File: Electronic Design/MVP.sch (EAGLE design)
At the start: 38 parts, among them IC1 ACS711KLCTR-12AB-T, IC3 ATMEGA328-PU, Q2 16MHz, Q3 IRF9540, Q4 IRF9540

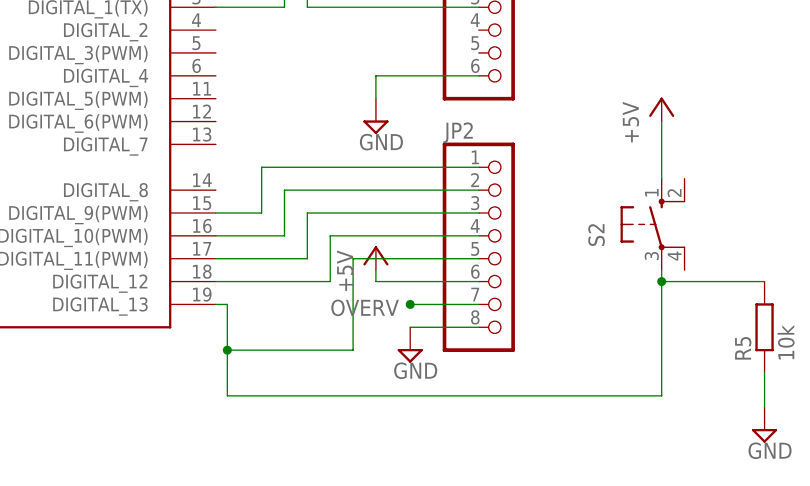
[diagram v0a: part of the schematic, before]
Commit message: Changed position of 5V and overvoltage on JP2
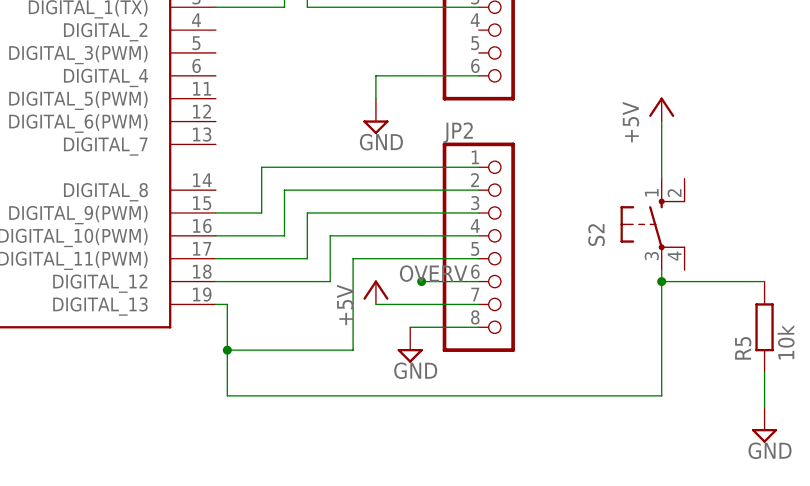
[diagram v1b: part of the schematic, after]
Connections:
- net +5V: now also JP2.7; no longer JP2.6
- net OVERV: now also JP2.6; no longer JP2.7
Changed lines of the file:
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@@
 <?xml version="1.0" encoding="utf-8"?>
 <!DOCTYPE eagle SYSTEM "eagle.dtd">
-<eagle version="7.6.0">
+<eagle version="7.5.0">
 <drawing>
 <settings>
@@
 <instance part="R5" gate="G$1" x="48.26" y="-10.16" rot="R90"/>
 <instance part="SUPPLY3" gate="GND" x="48.26" y="-21.59"/>
-<instance part="+5V3" gate="1" x="5.08" y="-1.27"/>
+<instance part="+5V3" gate="1" x="5.08" y="-5.08"/>
 <instance part="POT1" gate="G$1" x="-40.64" y="71.12" smashed="yes" rot="MR180">
 <attribute name="NAME" x="-39.37" y="65.151" size="1.778" layer="95" rot="MR180"/>
@@
 <segment>
 <pinref part="+5V3" gate="1" pin="+5V"/>
-<wire x1="5.08" y1="-3.81" x2="5.08" y2="-5.08" width="0.1524" layer="91"/>
-<pinref part="JP2" gate="A" pin="6"/>
-<wire x1="5.08" y1="-5.08" x2="16.51" y2="-5.08" width="0.1524" layer="91"/>
+<pinref part="JP2" gate="A" pin="7"/>
+<wire x1="5.08" y1="-7.62" x2="16.51" y2="-7.62" width="0.1524" layer="91"/>
 </segment>
 </net>
@@
 </segment>
 <segment>
-<pinref part="JP2" gate="A" pin="7"/>
-<wire x1="16.51" y1="-7.62" x2="8.89" y2="-7.62" width="0.1524" layer="91"/>
-<junction x="8.89" y="-7.62"/>
-<label x="0" y="-8.89" size="1.778" layer="95"/>
-</segment>
-</net>
+<pinref part="JP2" gate="A" pin="6"/>
+<wire x1="16.51" y1="-5.08" x2="10.16" y2="-5.08" width="0.1524" layer="91"/>
+<junction x="10.16" y="-5.08"/>
+<label x="7.62" y="-5.08" size="1.778" layer="95"/>
+</segment>
+</net>

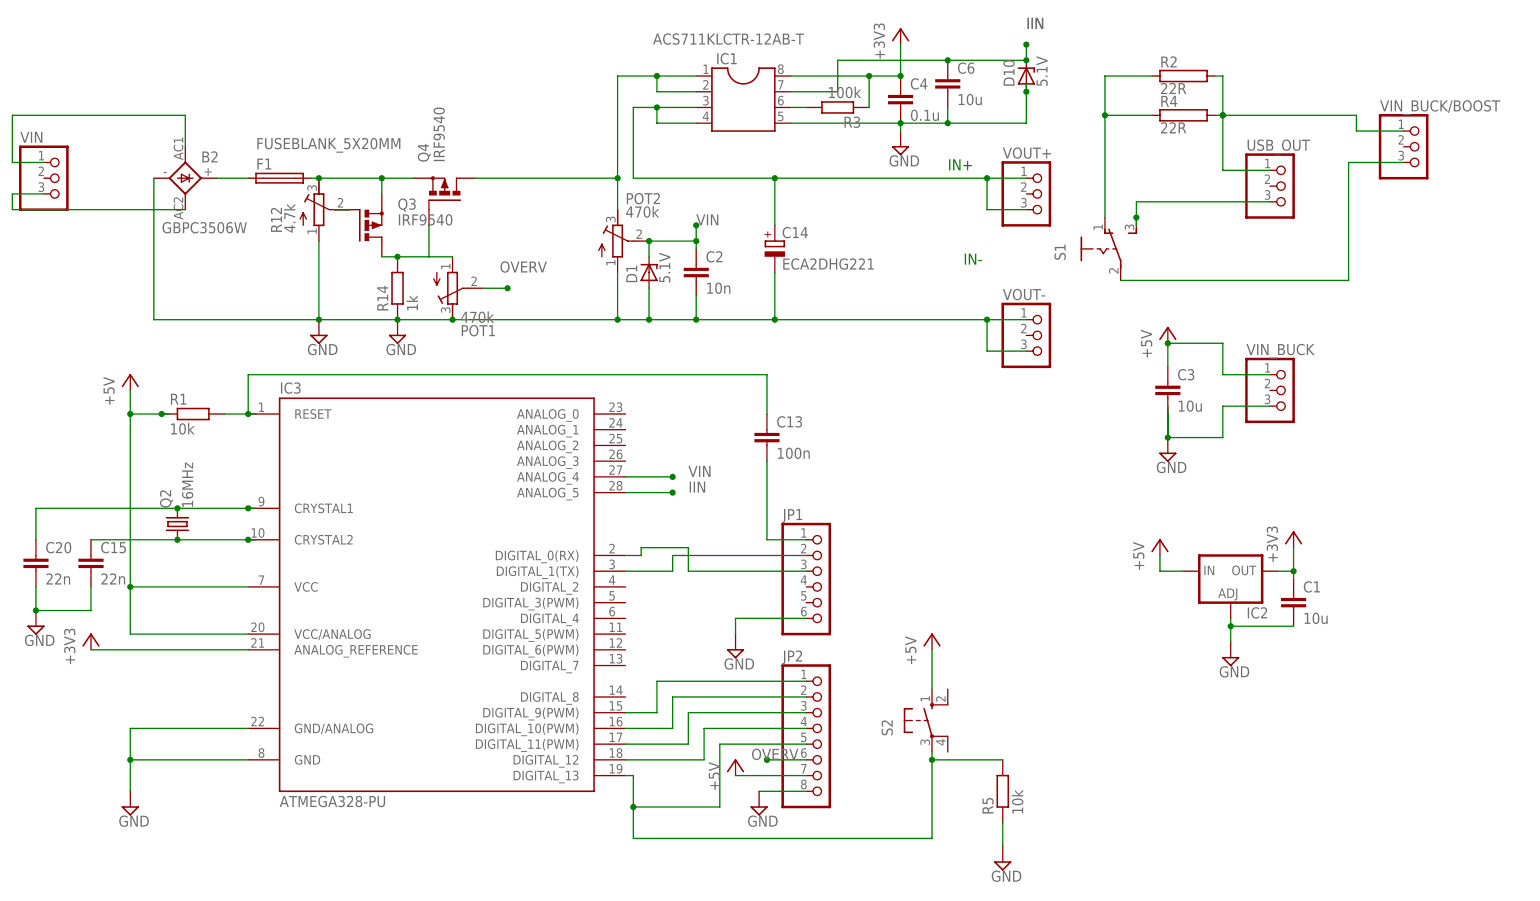
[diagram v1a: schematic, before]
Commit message: Updated circuit to reflect change from ACS711 to ACS712
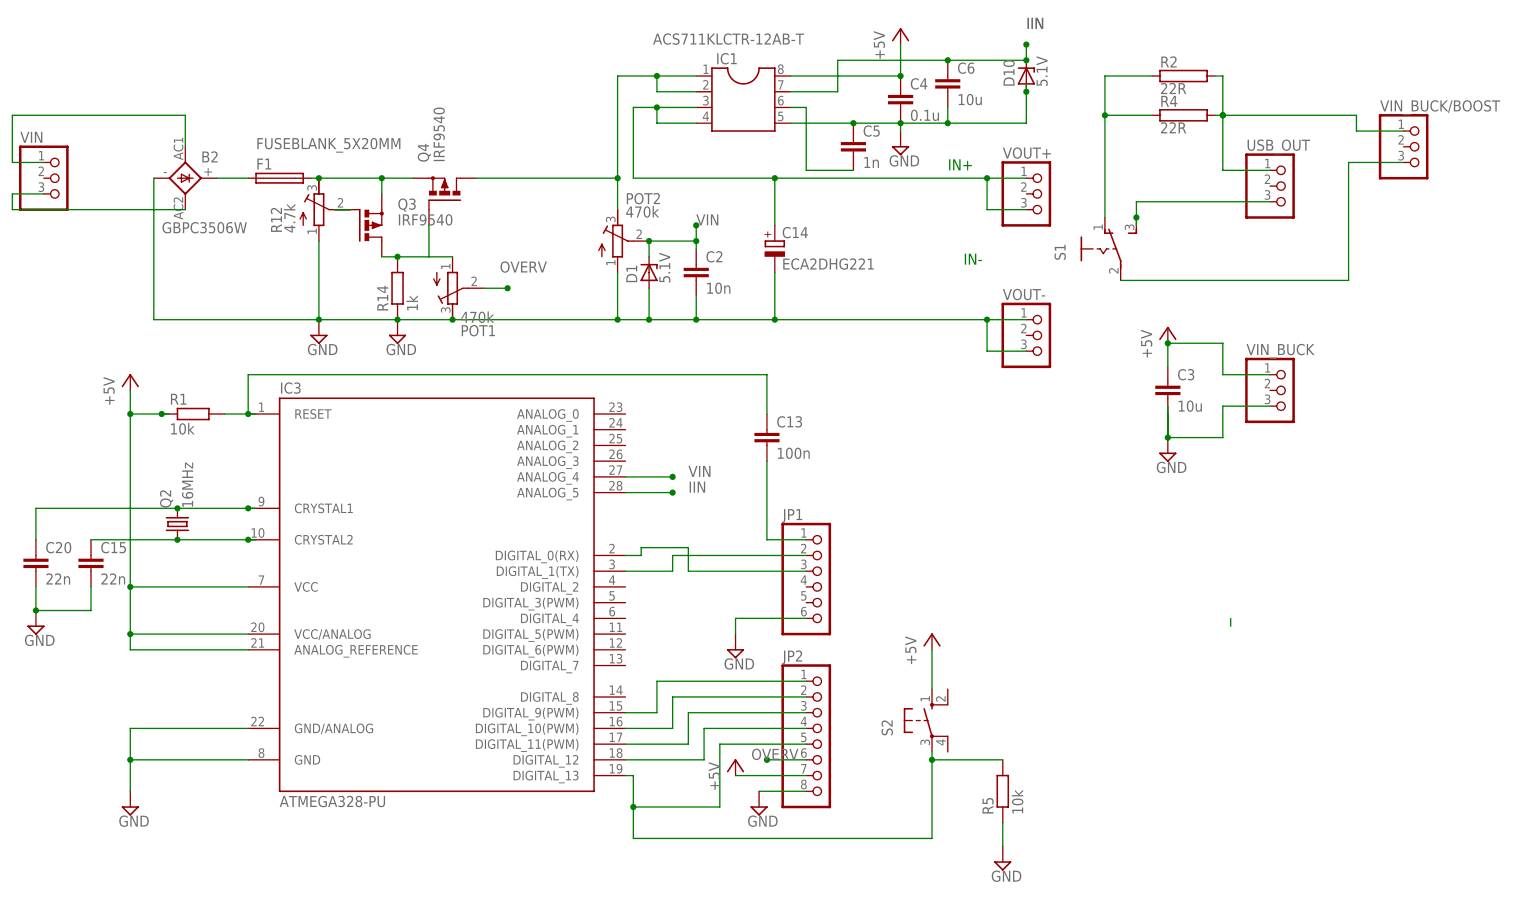
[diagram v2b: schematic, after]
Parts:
- removed C1: 10u, resistor:C-EUC1210
- removed IC2: (no value), v-reg:LM138-TS
- removed R3: 100k, resistor:R-EU_R1210
- added C5: 1n, resistor:C-EUC1210
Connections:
- removed net +3V3: C1.1, C4.1, IC1.8, IC2.OUT, IC3.ANALOG_REFERENCE, R3.1
- net +5V: now also C4.1, IC1.8, IC3.ANALOG_REFERENCE; no longer IC2.IN
- net GND: now also C5.1; no longer C1.2, IC2.ADJ
- net N$2: now also C5.2; no longer R3.2
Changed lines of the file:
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@@
 <part name="C4" library="resistor" deviceset="C-EU" device="C1210" value="0.1u"/>
 <part name="SUPPLY1" library="supply2" deviceset="GND" device=""/>
-<part name="R3" library="resistor" deviceset="R-EU_" device="R1210" value="100k"/>
 <part name="POT2" library="resistor" deviceset="R-TRIMM" device="4G/J" value="470k"/>
 <part name="D10" library="diode" deviceset="ZPD" device="" value="5.1V"/>
@@
 <part name="SUPPLY2" library="supply2" deviceset="GND" device=""/>
 <part name="+3V2" library="supply1" deviceset="+5V" device=""/>
-<part name="IC2" library="v-reg" deviceset="LM138-TS" device=""/>
-<part name="SUPPLY5" library="supply2" deviceset="GND" device=""/>
 <part name="+3V3" library="supply1" deviceset="+5V" device=""/>
-<part name="+3V4" library="supply1" deviceset="+3V3" device=""/>
-<part name="C1" library="resistor" deviceset="C-EU" device="C1210" value="10u"/>
-<part name="+3V1" library="supply1" deviceset="+3V3" device=""/>
-<part name="+3V5" library="supply1" deviceset="+3V3" device=""/>
 <part name="JP1" library="pinhead" deviceset="PINHD-1X6" device=""/>
 <part name="SUPPLY6" library="supply2" deviceset="GND" device=""/>
@@
 <part name="D1" library="diode" deviceset="ZPD" device="" value="5.1V"/>
 <part name="C6" library="resistor" deviceset="C-EU" device="C1210" value="10u"/>
+<part name="C5" library="resistor" deviceset="C-EU" device="C1210" value="1n"/>
 </parts>
 <sheets>
@@
 <instance part="C4" gate="G$1" x="31.75" y="102.87"/>
 <instance part="SUPPLY1" gate="GND" x="31.75" y="93.98"/>
-<instance part="R3" gate="G$1" x="21.59" y="100.33" rot="R180"/>
 <instance part="POT2" gate="G$1" x="-13.97" y="78.74" smashed="yes">
 <attribute name="NAME" x="-12.7" y="84.709" size="1.778" layer="95"/>
@@
 <instance part="SUPPLY2" gate="GND" x="74.93" y="44.45"/>
 <instance part="+3V2" gate="1" x="74.93" y="64.77"/>
-<instance part="IC2" gate="G$1" x="85.09" y="25.4"/>
-<instance part="SUPPLY5" gate="GND" x="85.09" y="11.43"/>
-<instance part="+3V3" gate="1" x="73.66" y="30.48"/>
-<instance part="+3V4" gate="G$1" x="95.25" y="31.75"/>
-<instance part="C1" gate="G$1" x="95.25" y="21.59"/>
-<instance part="+3V1" gate="G$1" x="31.75" y="113.03"/>
-<instance part="+3V5" gate="G$1" x="-99.06" y="15.24"/>
+<instance part="+3V3" gate="1" x="31.75" y="113.03"/>
 <instance part="JP1" gate="A" x="19.05" y="22.86"/>
 <instance part="SUPPLY6" gate="GND" x="5.08" y="12.7"/>
@@
 <instance part="D1" gate="G$1" x="-8.89" y="73.66" rot="R90"/>
 <instance part="C6" gate="G$1" x="39.37" y="105.41"/>
+<instance part="C5" gate="G$1" x="24.13" y="95.25"/>
 </instances>
 <busses>
@@
 <junction x="39.37" y="97.79"/>
 <pinref part="IC1" gate="G$1" pin="5"/>
-<wire x1="13.97" y1="97.79" x2="31.75" y2="97.79" width="0.1524" layer="91"/>
+<wire x1="13.97" y1="97.79" x2="24.13" y2="97.79" width="0.1524" layer="91"/>
+<wire x1="24.13" y1="97.79" x2="31.75" y2="97.79" width="0.1524" layer="91"/>
 <wire x1="31.75" y1="97.79" x2="31.75" y2="96.52" width="0.1524" layer="91"/>
 <pinref part="C6" gate="G$1" pin="2"/>
+<pinref part="C5" gate="G$1" pin="1"/>
+<junction x="24.13" y="97.79"/>
 </segment>
 <segment>
@@
 <pinref part="VIN_BUCK" gate="A" pin="3"/>
 <wire x1="83.82" y1="52.07" x2="91.44" y2="52.07" width="0.1524" layer="91"/>
-</segment>
-<segment>
-<pinref part="IC2" gate="G$1" pin="ADJ"/>
-<wire x1="85.09" y1="17.78" x2="85.09" y2="16.51" width="0.1524" layer="91"/>
-<pinref part="C1" gate="G$1" pin="2"/>
-<wire x1="85.09" y1="16.51" x2="85.09" y2="13.97" width="0.1524" layer="91"/>
-<wire x1="95.25" y1="16.51" x2="85.09" y2="16.51" width="0.1524" layer="91"/>
-<junction x="85.09" y="16.51"/>
-<pinref part="SUPPLY5" gate="GND" pin="GND"/>
 </segment>
 <segment>
@@
 <junction x="-87.63" y="50.8"/>
 <junction x="-92.71" y="50.8"/>
+<pinref part="IC3" gate="1" pin="ANALOG_REFERENCE"/>
+<wire x1="-73.66" y1="12.7" x2="-92.71" y2="12.7" width="0.1524" layer="91"/>
+<wire x1="-92.71" y1="12.7" x2="-92.71" y2="15.24" width="0.1524" layer="91"/>
+<junction x="-92.71" y="15.24"/>
 </segment>
 <segment>
@@
 </segment>
 <segment>
-<pinref part="IC2" gate="G$1" pin="IN"/>
-<pinref part="+3V3" gate="1" pin="+5V"/>
-<wire x1="77.47" y1="25.4" x2="73.66" y2="25.4" width="0.1524" layer="91"/>
-<wire x1="73.66" y1="25.4" x2="73.66" y2="27.94" width="0.1524" layer="91"/>
-</segment>
-<segment>
 <pinref part="S2" gate="1" pin="S"/>
 <pinref part="+5V2" gate="1" pin="+5V"/>
@@
 <wire x1="5.08" y1="-7.62" x2="16.51" y2="-7.62" width="0.1524" layer="91"/>
 </segment>
+<segment>
+<pinref part="C4" gate="G$1" pin="1"/>
+<wire x1="31.75" y1="105.41" x2="31.75" y2="110.49" width="0.1524" layer="91"/>
+<junction x="31.75" y="105.41"/>
+<pinref part="IC1" gate="G$1" pin="8"/>
+<wire x1="13.97" y1="105.41" x2="31.75" y2="105.41" width="0.1524" layer="91"/>
+<pinref part="+3V3" gate="1" pin="+5V"/>
+</segment>
 </net>
 <net name="N$1" class="0">
@@
 <pinref part="F1" gate="G$1" pin="1"/>
 <wire x1="-78.74" y1="88.9" x2="-73.66" y2="88.9" width="0.1524" layer="91"/>
-</segment>
-</net>
-<net name="N$2" class="0">
-<segment>
-<pinref part="R3" gate="G$1" pin="2"/>
-<pinref part="IC1" gate="G$1" pin="6"/>
-<wire x1="16.51" y1="100.33" x2="13.97" y2="100.33" width="0.1524" layer="91"/>
 </segment>
 </net>
@@
 </segment>
 </net>
-<net name="+3V3" class="0">
-<segment>
-<pinref part="IC2" gate="G$1" pin="OUT"/>
-<pinref part="+3V4" gate="G$1" pin="+3V3"/>
-<wire x1="92.71" y1="25.4" x2="95.25" y2="25.4" width="0.1524" layer="91"/>
-<wire x1="95.25" y1="25.4" x2="95.25" y2="29.21" width="0.1524" layer="91"/>
-<pinref part="C1" gate="G$1" pin="1"/>
-<wire x1="95.25" y1="24.13" x2="95.25" y2="25.4" width="0.1524" layer="91"/>
-<junction x="95.25" y="25.4"/>
-</segment>
-<segment>
-<pinref part="C4" gate="G$1" pin="1"/>
-<wire x1="26.67" y1="105.41" x2="31.75" y2="105.41" width="0.1524" layer="91"/>
-<pinref part="R3" gate="G$1" pin="1"/>
-<wire x1="26.67" y1="100.33" x2="26.67" y2="105.41" width="0.1524" layer="91"/>
-<wire x1="31.75" y1="105.41" x2="31.75" y2="110.49" width="0.1524" layer="91"/>
-<junction x="31.75" y="105.41"/>
-<pinref part="IC1" gate="G$1" pin="8"/>
-<wire x1="13.97" y1="105.41" x2="26.67" y2="105.41" width="0.1524" layer="91"/>
-<junction x="26.67" y="105.41"/>
-<pinref part="+3V1" gate="G$1" pin="+3V3"/>
-</segment>
-<segment>
-<pinref part="IC3" gate="1" pin="ANALOG_REFERENCE"/>
-<pinref part="+3V5" gate="G$1" pin="+3V3"/>
-<wire x1="-73.66" y1="12.7" x2="-99.06" y2="12.7" width="0.1524" layer="91"/>
-</segment>
-</net>
 <net name="N$4" class="0">
 <segment>
@@
 </segment>
 </net>
+<net name="N$7" class="0">
+<segment>
+<wire x1="85.09" y1="17.78" x2="85.09" y2="16.51" width="0.1524" layer="91"/>
+</segment>
+</net>
+<net name="N$2" class="0">
+<segment>
+<pinref part="C5" gate="G$1" pin="2"/>
+<wire x1="24.13" y1="90.17" x2="16.51" y2="90.17" width="0.1524" layer="91"/>
+<wire x1="16.51" y1="90.17" x2="16.51" y2="100.33" width="0.1524" layer="91"/>
+<pinref part="IC1" gate="G$1" pin="6"/>
+<wire x1="16.51" y1="100.33" x2="13.97" y2="100.33" width="0.1524" layer="91"/>
+</segment>
+</net>

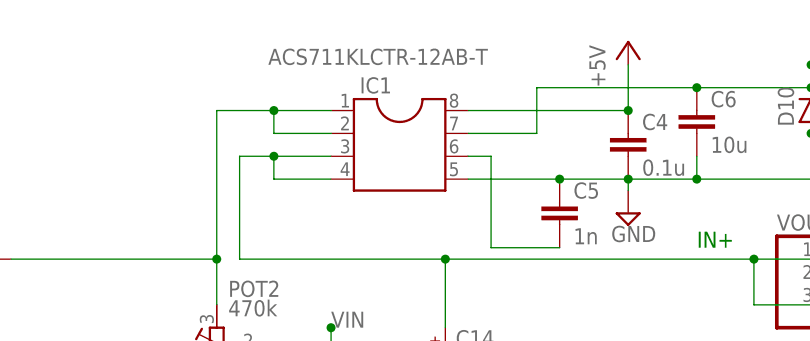
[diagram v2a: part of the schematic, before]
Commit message: Changing name of IC1 to reflect change of current sensing module
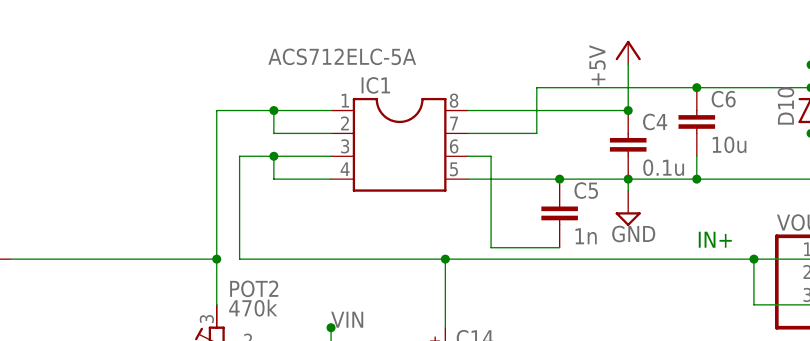
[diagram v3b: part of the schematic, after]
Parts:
- IC1: value ACS711KLCTR-12AB-T -> ACS712ELC-5A
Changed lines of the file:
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@@
 <setting verticaltext="up"/>
 </settings>
-<grid distance="0.05" unitdist="inch" unit="inch" style="lines" multiple="1" display="no" altdistance="0.01" altunitdist="inch" altunit="inch"/>
+<grid distance="0.1" unitdist="inch" unit="inch" style="lines" multiple="1" display="no" altdistance="0.01" altunitdist="inch" altunit="inch"/>
 <layers>
 <layer number="1" name="Top" color="4" fill="1" visible="no" active="no"/>
@@
 <part name="C2" library="resistor" deviceset="C-EU" device="C1210" value="10n"/>
 <part name="C14" library="rcl" deviceset="CPOL-EU" device="E7.5-18" value="ECA2DHG221"/>
-<part name="IC1" library="mylibrary" deviceset="SOIC8" device="" value="ACS711KLCTR-12AB-T"/>
+<part name="IC1" library="mylibrary" deviceset="SOIC8" device="" value="ACS712ELC-5A"/>
 <part name="C4" library="resistor" deviceset="C-EU" device="C1210" value="0.1u"/>
 <part name="SUPPLY1" library="supply2" deviceset="GND" device=""/>
